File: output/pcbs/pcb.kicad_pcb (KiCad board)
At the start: 2 copper layers, 131.6 x 93.2 mm, 48 parts

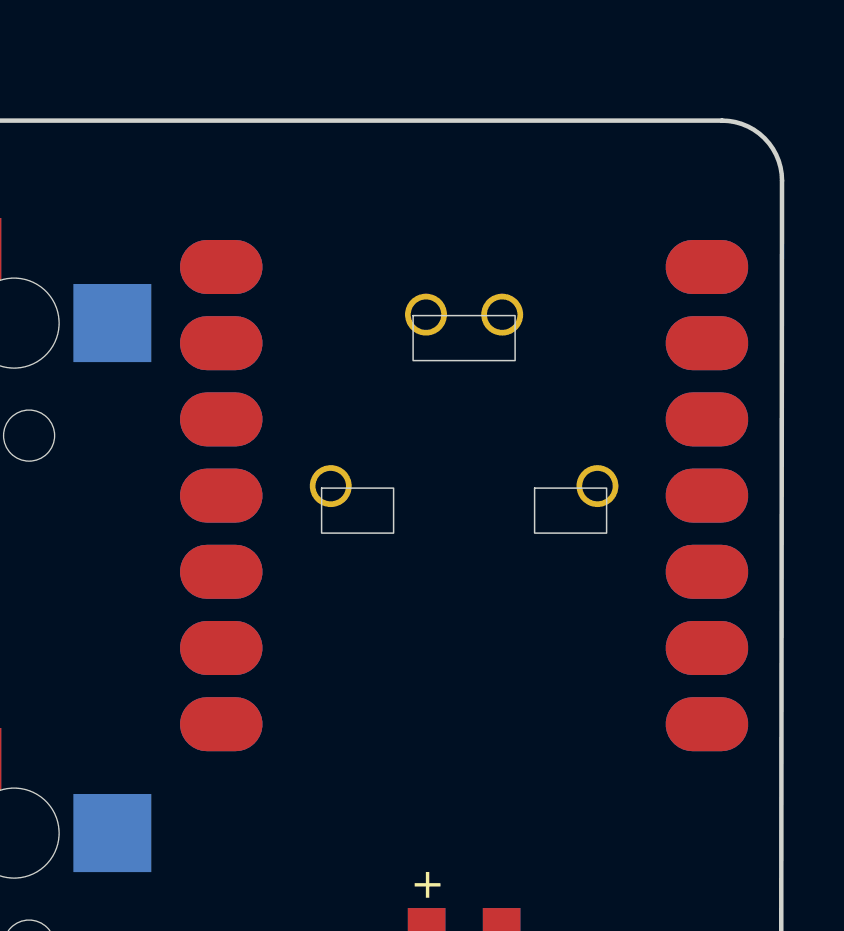
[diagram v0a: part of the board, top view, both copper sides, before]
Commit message: dev: add kicad outputs
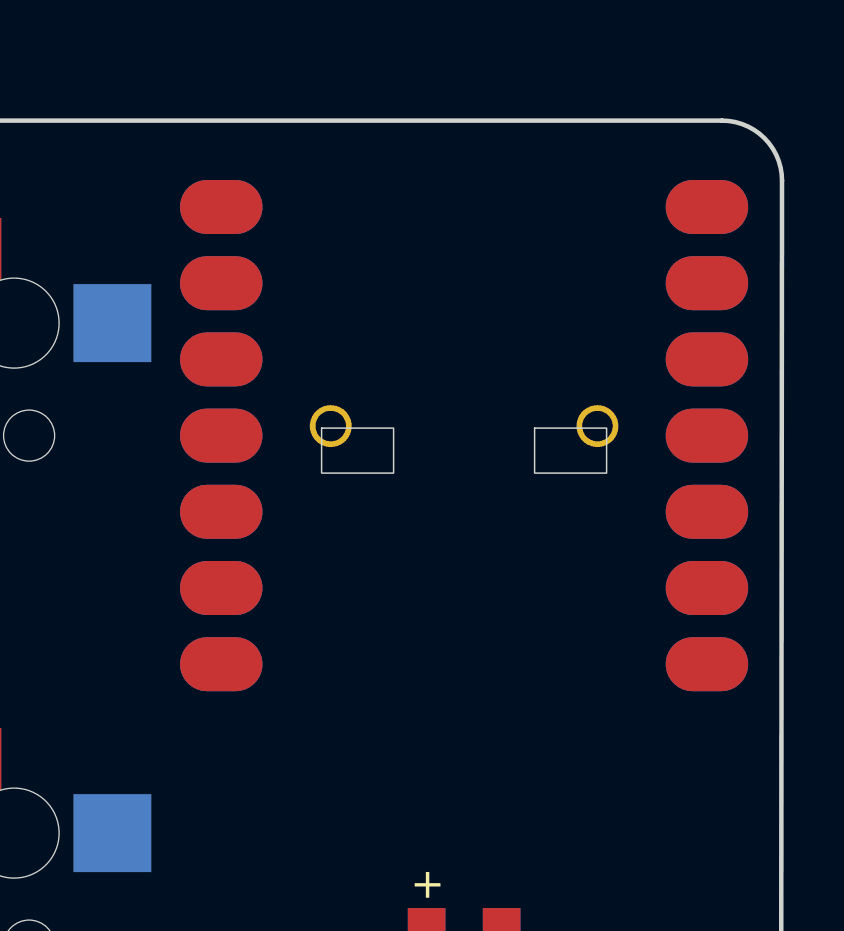
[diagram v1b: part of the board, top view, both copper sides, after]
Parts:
- moved MCU1 2.00 mm to (280.0, 121.0)
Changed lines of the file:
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@@
     (module "xiao-ble-smd-reversible"
       (layer "F.Cu")
-      (at 280 123 0)
+      (at 280 121 0)
       (attr smd exclude_from_pos_files)
       (fp_text reference "MCU1" (at 0 0) (layer F.SilkS) hide (effects (font (size 1.27 1.27) (thickness 0.15))))
@@
       (fp_rect (start -4.75 -0.25) (end -2.35 1.25)
         (stroke (width 0.05) (type default)) (fill none) (layer "Edge.Cuts"))
-      (fp_rect (start -1.7 -6) (end 1.7 -4.5)
-        (stroke (width 0.05) (type default)) (fill none) (layer "Edge.Cuts"))
       (fp_rect (start 2.35 -0.25) (end 4.75 1.25)
         (stroke (width 0.05) (type default)) (fill none) (layer "Edge.Cuts"))
@@
       (pad "14" smd oval (at -8.56996 -7.62) (size 2.75 1.8) (drill (offset 0.475 0)) (layers "B.Cu" "B.Paste" "B.Mask") (net 34 "5V"))
       (pad "14" smd oval (at 8.56996 -7.62) (size 2.75 1.8) (drill (offset -0.475 0)) (layers "F.Cu" "F.Paste" "F.Mask") (net 34 "5V"))
-      (pad "17" thru_hole circle (at -1.27 -6.032 90) (size 1.397 1.397) (drill 1.016) (property pad_prop_castellated) (layers *.Cu *.Mask) (net 33 "GND"))
-      (pad "18" thru_hole circle (at 1.27 -6.032 270) (size 1.397 1.397) (drill 1.016) (property pad_prop_castellated) (layers *.Cu *.Mask) (net 35 "RST"))
       (pad "19" thru_hole circle (at 4.445 -0.317 180) (size 1.397 1.397) (drill 1.016) (property pad_prop_castellated) (layers *.Cu *.Mask) (net 36 "BAT+"))
       (pad "19" thru_hole circle (at -4.445 -0.317 180) (size 1.397 1.397) (drill 1.016) (property pad_prop_castellated) (layers *.Cu *.Mask) (net 36 "BAT+"))
